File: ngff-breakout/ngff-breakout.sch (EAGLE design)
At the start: 43 parts, among them K1 694108106102, U1 IP4234CZ6, U2 LD1085D2T33R, X2 MINI-USB-SHIELD-UX60-MB-5ST

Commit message: ngff-breakout: intermediate state
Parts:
- removed C105, C109: 100u, rc-sysmocom:CAP_CERAMIC1206
- removed C106, C110: 100n, rc-sysmocom:CAP_CERAMIC_0603
- removed C107, C111: 33p, rc-sysmocom:CAP_CERAMIC_0402
- removed C108, C112: 10p, rc-sysmocom:CAP_CERAMIC_0603
- removed X4, X5: (no value), laforge:SMA-F-S-TH
- removed Y4, Y5: (no value), laforge:HRS_UFL
- added C12, C17: 10u, rc-sysmocom:CAP_CERAMIC_0805
- added C13: 100u, rc-sysmocom:CAP_CERAMIC1206
- added C14, C19: 100n, rc-sysmocom:CAP_CERAMIC_0603
- added C15: 33p, rc-sysmocom:CAP_CERAMIC_0402
- added C16: 10p, rc-sysmocom:CAP_CERAMIC_0603
- added C18: DNP, rcl:CPOL-EUSMCE
- added CN1: (no value), USB30B:USB3.0-B
- added CN2: (no value), USB30-MICROB:USB3.0-MICROB
- added X1: (no value), laforge:SMA-F-S-TH
- added Y1, Y2: (no value), laforge:HRS_UFL
- C1: value 10u -> 100n; device rc-sysmocom:CAP_CERAMIC_0805 -> rc-sysmocom:CAP_CERAMIC_0603; DESCRIPTION 10µF 16V Ceramic Capacitor X5R 0805 (2012 Metric) 0.079" L 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 -> CAP CER 0.1UF 16V 10% X7R 0603; LINK http://www.digikey.com/product-detail/en/samsung-electro-me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 -> http://www.digikey.com/product-detail/en/foo/1276-1005-1-ND; MANUFACTURER Samsung Electro-Mechanics America, Inc. -> Samsung Electro-Mechanics America, Inc; MANUFACTURERPARTNUMBER CL21A106KOQNNNG -> CL10B104KO8NNNC; ROHSCERTIFICATE UNKNOWN ROHS CERTIFICATE -> Bleifrei / RoHS-konform; SOURCEPARTNUMBER 1276-6455-1-ND -> 1276-1005-1-ND
- C10: value 100u -> 470u; device rc-sysmocom:CAP_CERAMIC1206 -> rcl:CPOL-EUUD-8X10; DESCRIPTION 100µF 6.3V Ceramic Capacitor X5R 1206 (3216 Metric) 0.126" 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 -> 470µF 6.3V Aluminum Capacitors Radial, Can - SMD 2000 Hrs @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; LINK http://www.digikey.com/product-detail/en/murata-electronics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 -> http://www.digikey.com/product-detail/en/nichicon/UUR0J471M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; MANUFACTURER Murata Electronics North America -> Nichicon; MANUFACTURERPARTNUMBER GRM31CR60J107ME39K -> UUR0J471MNL1GS; SOURCEPARTNUMBER 490-7217-1-ND -> 493-6207-1-ND
- C2: value 10u -> 33p; device rc-sysmocom:CAP_CERAMIC_0805 -> rc-sysmocom:CAP_CERAMIC_0402; DESCRIPTION 10µF 16V Ceramic Capacitor X5R 0805 (2012 Metric) 0.079" L 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 -> CAP CER 33PF 50V NP0 0402; LINK http://www.digikey.com/product-detail/en/samsung-electro-me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 -> http://www.digikey.com/product-detail/en/CL05C330JB5NNNC/12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; MANUFACTURERPARTNUMBER CL21A106KOQNNNG -> CL05C330JB5NNNC; ROHSCERTIFICATE UNKNOWN ROHS CERTIFICATE -> Bleifrei / RoHS-konform; SOURCEPARTNUMBER 1276-6455-1-ND -> 1276-1272-1-ND
- C3: value 470u -> 33p; device rcl:CPOL-EUUD-8X10 -> rc-sysmocom:CAP_CERAMIC_0402; DESCRIPTION 470µF 6.3V Aluminum Capacitors Radial, Can - SMD 2000 Hrs @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 -> CAP CER 33PF 50V NP0 0402; LINK http://www.digikey.com/product-detail/en/nichicon/UUR0J471M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 -> http://www.digikey.com/product-detail/en/CL05C330JB5NNNC/12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; MANUFACTURER Nichicon -> Samsung Electro-Mechanics America, Inc.; MANUFACTURERPARTNUMBER UUR0J471MNL1GS -> CL05C330JB5NNNC; ROHSCERTIFICATE UNKNOWN ROHS CERTIFICATE -> Bleifrei / RoHS-konform; SOURCEPARTNUMBER 493-6207-1-ND -> 1276-1272-1-ND
- C4: value DNP -> 33p; device rcl:CPOL-EUSMCE -> rc-sysmocom:CAP_CERAMIC_0402; DESCRIPTION NO DESCRIPTION -> CAP CER 33PF 50V NP0 0402; LINK UNKNOWN LINK -> http://www.digikey.com/product-detail/en/CL05C330JB5NNNC/12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; MANUFACTURER UNKNOWN MANUFACTURER -> Samsung Electro-Mechanics America, Inc.; MANUFACTURERPARTNUMBER UNKNOWN MANUFACTURER PART NUMBER -> CL05C330JB5NNNC; POPULATED FALSE -> TRUE; ROHSCERTIFICATE UNKNOWN ROHS CERTIFICATE -> Bleifrei / RoHS-konform; SOURCE UNKNOWN SOURCE -> DIGIKEY; SOURCEPARTNUMBER UNKNOWN SOURCE PART NUMBER -> 1276-1272-1-ND
- C5, C6: value 33p -> 100u; device rc-sysmocom:CAP_CERAMIC_0402 -> rc-sysmocom:CAP_CERAMIC1206; DESCRIPTION CAP CER 33PF 50V NP0 0402 -> 100µF 6.3V Ceramic Capacitor X5R 1206 (3216 Metric) 0.126" 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; LINK http://www.digikey.com/product-detail/en/CL05C330JB5NNNC/12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 -> http://www.digikey.com/product-detail/en/murata-electronics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; MANUFACTURER Samsung Electro-Mechanics America, Inc. -> Murata Electronics North America; MANUFACTURERPARTNUMBER CL05C330JB5NNNC -> GRM31CR60J107ME39K; ROHSCERTIFICATE Bleifrei / RoHS-konform -> UNKNOWN ROHS CERTIFICATE; SOURCEPARTNUMBER 1276-1272-1-ND -> 490-7217-1-ND
- C7: value 33p -> 100n; device rc-sysmocom:CAP_CERAMIC_0402 -> rc-sysmocom:CAP_CERAMIC_0603; DESCRIPTION CAP CER 33PF 50V NP0 0402 -> CAP CER 0.1UF 16V 10% X7R 0603; LINK http://www.digikey.com/product-detail/en/CL05C330JB5NNNC/12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 -> http://www.digikey.com/product-detail/en/foo/1276-1005-1-ND; MANUFACTURER Samsung Electro-Mechanics America, Inc. -> Samsung Electro-Mechanics America, Inc; MANUFACTURERPARTNUMBER CL05C330JB5NNNC -> CL10B104KO8NNNC; SOURCEPARTNUMBER 1276-1272-1-ND -> 1276-1005-1-ND
- C8: value 100n -> 33p; device rc-sysmocom:CAP_CERAMIC_0603 -> rc-sysmocom:CAP_CERAMIC_0402; DESCRIPTION CAP CER 0.1UF 16V 10% X7R 0603 -> CAP CER 33PF 50V NP0 0402; LINK http://www.digikey.com/product-detail/en/foo/1276-1005-1-ND -> http://www.digikey.com/product-detail/en/CL05C330JB5NNNC/12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; MANUFACTURER Samsung Electro-Mechanics America, Inc -> Samsung Electro-Mechanics America, Inc.; MANUFACTURERPARTNUMBER CL10B104KO8NNNC -> CL05C330JB5NNNC; SOURCEPARTNUMBER 1276-1005-1-ND -> 1276-1272-1-ND
- C9: value 100n -> 10p; DESCRIPTION CAP CER 0.1UF 16V 10% X7R 0603 -> CAP CER 10PF 50V NP0 0603; LINK http://www.digikey.com/product-detail/en/foo/1276-1005-1-ND -> http://www.digikey.com/product-detail/en/C0603C100J5GACTU/3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; MANUFACTURER Samsung Electro-Mechanics America, Inc -> Kemet; MANUFACTURERPARTNUMBER CL10B104KO8NNNC -> C0603C100J5GACTU; SOURCEPARTNUMBER 1276-1005-1-ND -> 399-1049-1-ND
- JP3: device jumper:JP2E -> pinhead:PINHD-2X12; DESCRIPTION NO DESCRIPTION -> 24 Positions Header, Unshrouded Connector 0.100" (2.54mm) T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; LINK UNKNOWN LINK -> http://www.digikey.com/product-detail/en/961224-6404-AR/3M9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; MANUFACTURER UNKNOWN MANUFACTURER -> 3M; MANUFACTURERPARTNUMBER UNKNOWN MANUFACTURER PART NUMBER -> 961224-6404-AR; SOURCE UNKNOWN SOURCE -> DIGIKEY; SOURCEPARTNUMBER UNKNOWN SOURCE PART NUMBER -> 3M9463-ND
- JP4: device pinhead:PINHD-2X12 -> jumper:JP2E; DESCRIPTION 24 Positions Header, Unshrouded Connector 0.100" (2.54mm) T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 -> NO DESCRIPTION; LINK http://www.digikey.com/product-detail/en/961224-6404-AR/3M9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 -> UNKNOWN LINK; MANUFACTURER 3M -> UNKNOWN MANUFACTURER; MANUFACTURERPARTNUMBER 961224-6404-AR -> UNKNOWN MANUFACTURER PART NUMBER; SOURCE DIGIKEY -> UNKNOWN SOURCE; SOURCEPARTNUMBER 3M9463-ND -> UNKNOWN SOURCE PART NUMBER
- LED1: value YELLOW -> GREEN
- LED2: value GREEN -> YELLOW
- R1, R2: value 47 -> 330; DESCRIPTION RES SMD 47 OHM 5% 1/10W 0603 -> RES SMD 330 OHM 5% 1/10W 0603; LINK http://www.digikey.com/product-detail/en/yageo/RC0603JR-074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 -> http://www.digikey.com/product-detail/en/yageo/RC0603JR-073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; MANUFACTURERPARTNUMBER RC0603JR-0747RL -> RC0603JR-07330RL; SOURCEPARTNUMBER 311-47GRCT-ND -> 311-330GRCT-ND
- R4: value 1M -> 47; DESCRIPTION RES SMD 1M OHM 5% 1/10W 0603 -> RES SMD 47 OHM 5% 1/10W 0603; LINK http://www.digikey.com/product-detail/en/yageo/RC0603JR-071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 -> http://www.digikey.com/product-detail/en/yageo/RC0603JR-074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; MANUFACTURERPARTNUMBER RC0603JR-071ML -> RC0603JR-0747RL; SOURCEPARTNUMBER 311-1.0MGRCT-ND -> 311-47GRCT-ND
- R5: value 330 -> 47; DESCRIPTION RES SMD 330 OHM 5% 1/10W 0603 -> RES SMD 47 OHM 5% 1/10W 0603; LINK http://www.digikey.com/product-detail/en/yageo/RC0603JR-073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 -> http://www.digikey.com/product-detail/en/yageo/RC0603JR-074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; MANUFACTURERPARTNUMBER RC0603JR-07330RL -> RC0603JR-0747RL; SOURCEPARTNUMBER 311-330GRCT-ND -> 311-47GRCT-ND
- R6: value 330 -> 1M; DESCRIPTION RES SMD 330 OHM 5% 1/10W 0603 -> RES SMD 1M OHM 5% 1/10W 0603; LINK http://www.digikey.com/product-detail/en/yageo/RC0603JR-073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 -> http://www.digikey.com/product-detail/en/yageo/RC0603JR-071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; MANUFACTURERPARTNUMBER RC0603JR-07330RL -> RC0603JR-071ML; SOURCEPARTNUMBER 311-330GRCT-ND -> 311-1.0MGRCT-ND
- X2: value MINI-USB-SHIELD-UX60-MB-5ST -> (none); device con-hirose:MINI-USB-SHIELD-UX60-MB-5ST -> laforge:SMA-F-S-TH; DESCRIPTION USB - mini B USB 2.0 Receptacle Connector 5 Position Surfac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 -> CONN SMA JACK STR 50 OHM PCB; LINK http://www.digikey.com/product-detail/en/hirose-electric-co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 -> http://www.digikey.com/product-detail/en/te-connectivity-am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; MANUFACTURER Hirose Electric Co Ltd -> TE Connectivity AMP Connectors; MANUFACTURERPARTNUMBER UX60-MB-5ST -> 5-1814832-1; SOURCEPARTNUMBER H2959CT-ND -> A97594-ND
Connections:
- removed net N$14 (its old number): X4.1, Y4.1
- new net N$11: CN1.TX+
- new net N$13: X2.1, Y2.1
- new net N$15: CN1.GND@1
- new net N$17: CN1.RX-
- new net N$18: CN1.RX+
- new net N$4: CN1.TX-
- new net USB3.0_RX_N: NGFF1G$1.USB3.0_RX_N
- new net USB3.0_RX_P: NGFF1G$1.USB3.0_RX_P
- new net USB3.0_TX_N: NGFF1G$1.USB3.0_TX_N
- new net USB3.0_TX_P: NGFF1G$1.USB3.0_TX_P
- net !CLKREQ: now also JP3.6; no longer JP4.6
- net COEX1: now also JP3.4; no longer JP4.4
- net COEX2: now also JP3.3; no longer JP4.3
- net GND: now also C10.-, C12.1, C13.1, C14.1, C15.2, C16.2, C17.1, C18.-, C19.1, C2.2, C3.2, C4.2, C5.1, C6.1, C7.1, C8.2, C9.2, CN1.GND@0, JP1.1, JP2.2, JP3.1, JP3.13, R1.1, R6.1, X1.GND@1, X1.GND@2, X1.GND@3, X1.GND@4, X2.GND@1, X2.GND@2, X2.GND@3, X2.GND@4, Y1.GND@1, Y1.GND@2, Y2.GND@1, Y2.GND@2; no longer C10.1, C105.1, C106.1, C107.2, C108.2, C109.1, C110.1, C111.2, C112.2, C2.1, C3.-, C4.-, C5.2, C6.2, C7.2, C8.1, C9.1, JP1.2, JP2.1, JP4.1, JP4.13, R4.1, R5.1, X2G$1.5, X4.GND@1, X4.GND@2, X4.GND@3, X4.GND@4, X5.GND@1, X5.GND@2, X5.GND@3, X5.GND@4, Y4.GND@1, Y4.GND@2, Y5.GND@1, Y5.GND@2
- net LDO_IN: now also C10.+, C12.2, JP4.2; no longer C1.2, C3.+, JP3.2
- net LED_WLAN: now also JP3.24; no longer JP4.24
- net LED_WPAN: now also JP3.23; no longer JP4.23
- net N$1: now also LED1.C, R1.2; no longer LED2.C, R5.2
- net N$10: now also C19.2, CN1.S1, CN1.S2, R6.2; no longer C9.2, R4.2, X2S.S1, X2S.S2, X2S.S3, X2S.S4
- net N$12: now also JP4.3; no longer JP3.3
- net N$16: now also JP3.11; no longer JP4.11
- net N$2: now also LED2.C, R2.1; no longer LED1.C, R6.1
- net N$3: now also R2.2; no longer R6.2
- net N$5: now also R5.1; no longer R1.1
- net N$7: now also X1.1, Y1.1; no longer X5.1, Y5.1
- net N$8: now also R3.1; no longer R2.1
- net N$9: now also R4.1; no longer R3.1
- net PERN0: now also JP3.9; no longer JP4.9
- net PERP0: now also JP3.12; no longer JP4.12
- net PERST: now also JP2.1; no longer JP1.1
- net PETN0: now also JP3.16; no longer JP4.16
- net PETP0: now also JP3.15; no longer JP4.15
- net REFCLK+: now also JP3.8; no longer JP4.8
- net REFCLK-: now also JP3.5; no longer JP4.5
- net RSVRD45: now also JP3.18; no longer JP4.18
- net RSVRD47: now also JP3.17; no longer JP4.17
- net RSVRD49: now also JP3.20; no longer JP4.20
- net RSVRD51: now also JP3.19; no longer JP4.19
- net SMB_CLK: now also JP3.21; no longer JP4.21
- net SMB_DATA: now also JP3.22; no longer JP4.22
- net UIM_C4: now also JP3.10; no longer JP4.10
- net UIM_C8: now also JP3.7; no longer JP4.7
- net USB_VBUS: now also CN1.VBUS, JP4.1; no longer JP3.1, X2G$1.1
- net USIM_CLK: now also C3.1, R3.2; no longer C5.1, R2.2
- net USIM_DATA: now also C4.1, R5.2; no longer C7.1, R1.2
- net USIM_POWER: now also C1.2; no longer C8.2
- net USIM_RESET: now also C2.1, R4.2; no longer C6.1, R3.2
- net VCC_3V3: now also C13.2, C14.2, C15.1, C16.1, C17.2, C18.+, C5.2, C6.2, C7.2, C8.1, C9.1, JP3.14; no longer C10.2, C105.2, C106.2, C107.1, C108.1, C109.2, C110.2, C111.1, C112.1, C2.2, C4.+, JP4.14
- net WAKE: now also JP3.2; no longer JP4.2
- net W_DISABLE: now also JP1.2; no longer JP2.2
- net _USB_D_N: now also CN1.D-; no longer X2G$1.2
- net _USB_D_P: now also CN1.D+; no longer X2G$1.3
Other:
- moved on the sheet: C1, C11, C2, C5, C6, C7, C8, C9, JP1, JP2, K1, LED1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

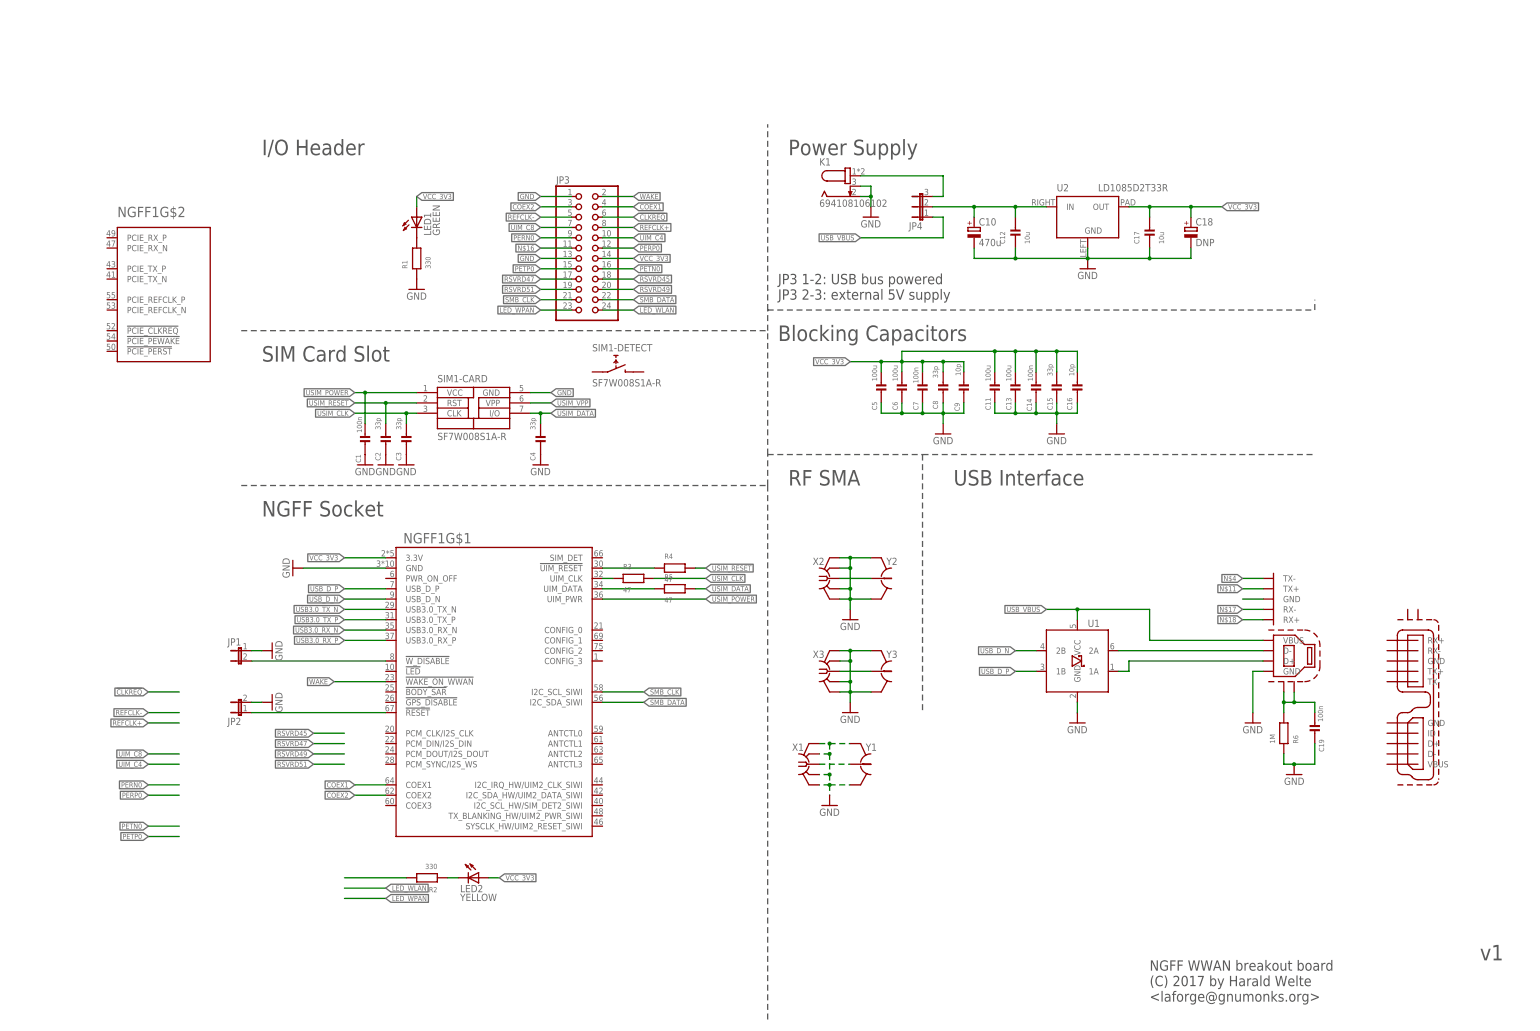
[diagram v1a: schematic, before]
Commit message: ngff-breakout: almost ready
missing: more vias, more ext. attributes (for BOM)
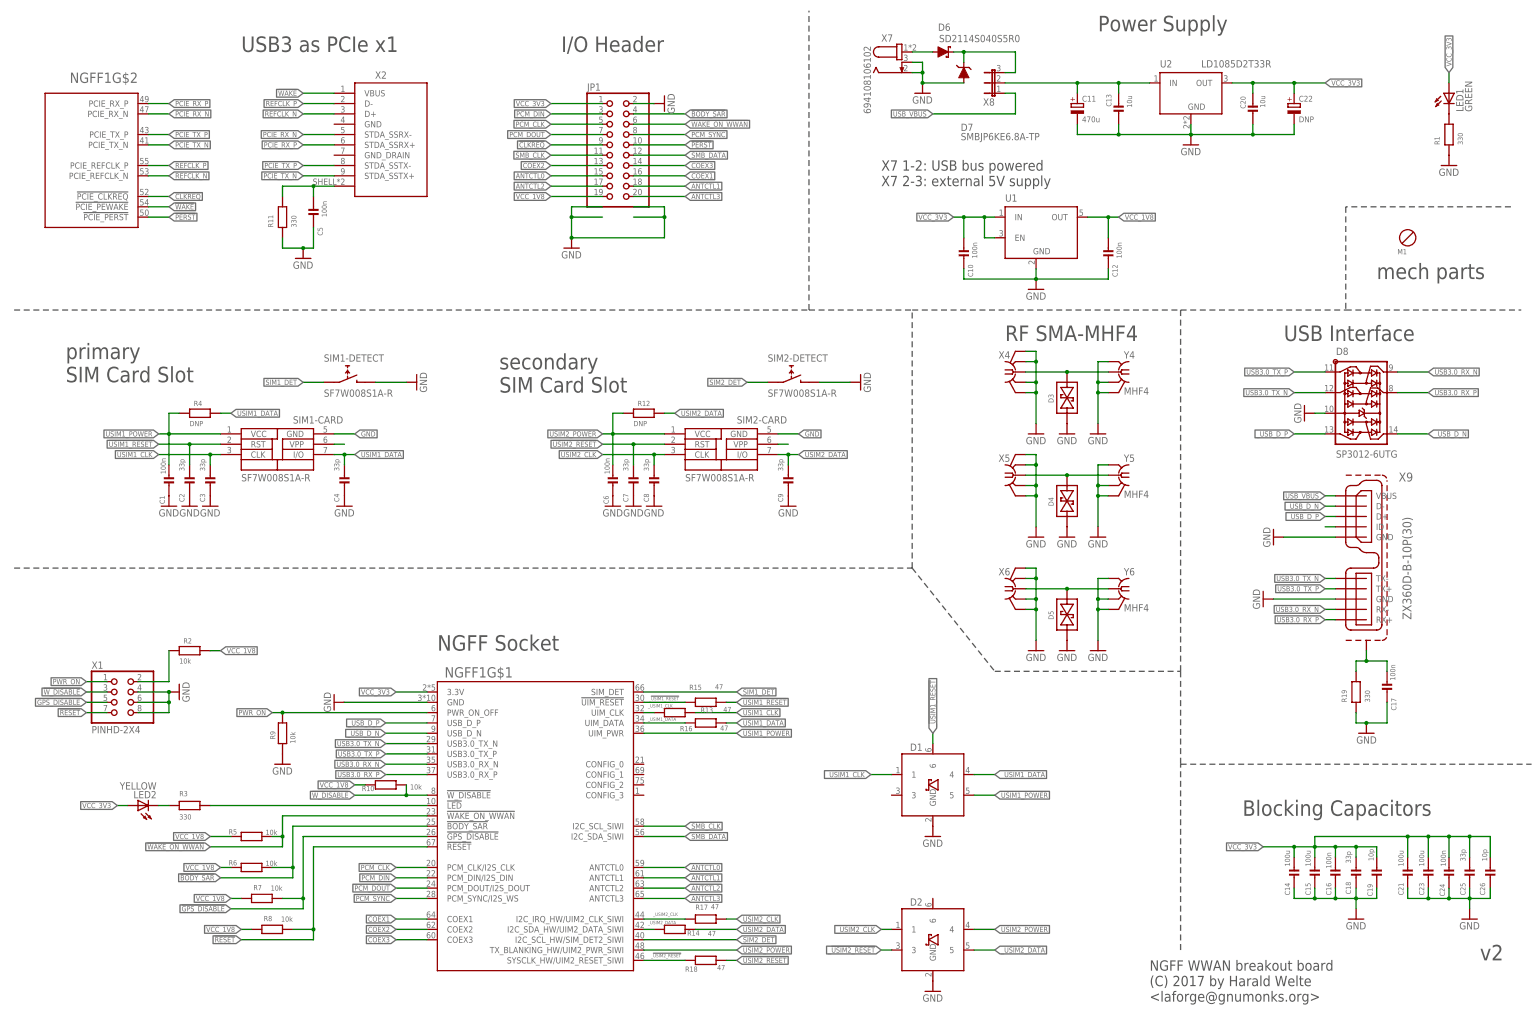
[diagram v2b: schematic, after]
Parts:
- removed CN1: (no value), USB30B:USB3.0-B
- removed CN2: (no value), USB30-MICROB:USB3.0-MICROB
- removed JP2: (no value), jumper:JP1E
- removed JP3: (no value), pinhead:PINHD-2X12
- removed JP4: (no value), jumper:JP2E
- removed K1: 694108106102, Wurth_Elektronik_Electromechanic_DC_Power_Jack_Connectors_rev15c:694108106102
- removed X3: (no value), laforge:SMA-F-S-TH
- removed Y1, Y2, Y3: (no value), laforge:HRS_UFL
- added C20: 10u, rc-sysmocom:CAP_CERAMIC_0805
- added C21, C23: 100u, rc-sysmocom:CAP_CERAMIC1206
- added C22: DNP, rcl:CPOL-EUSMCE
- added C24: 100n, rc-sysmocom:CAP_CERAMIC_0603
- added C25: 33p, rc-sysmocom:CAP_CERAMIC_0402
- added C26: 10p, rc-sysmocom:CAP_CERAMIC_0603
- added D1, D2: PESD5V0UBV, laforge:PESD5V0UBV
- added D3, D4, D5: GG040205170N2P, diodes-sysmocom:TVSDIODE-BIDI-0402
- added D6: SD2114S040S5R0, diodes-sysmocom:DIODE-SCHOTTKY-SMB
- added D7: SMBJP6KE6.8A-TP, diodes-sysmocom:DIODE-TVS-SMB
- added D8: SP3012-6UTG, SP3012:SP3012-6UTG
- added R10, R7, R8, R9: 10k, rc-sysmocom:RESISTOR_0603
- added R11, R19: 330, rc-sysmocom:RESISTOR_0603
- added R12: DNP, rc-sysmocom:RESISTOR_0603
- added R13, R14, R15, R16, R17, R18: 47, rc-sysmocom:RESISTOR_0402
- added SIM2: SF7W008S1A-R, SF7W008S1A-SIM:SF7W008S1A-R
- added X4, X5, X6: (no value), laforge:SMA-F-S-TH
- added X7: 694108106102, Wurth_Elektronik_Electromechanic_DC_Power_Jack_Connectors_rev15c:694108106102
- added X8: (no value), jumper:JP2E
- added X9: ZX360D-B-10P(30), USB30-MICROB:USB3.0-MICROB
- added Y4, Y5, Y6: MHF4, con-MHF4:MHF4
- C1: LINK http://www.digikey.com/product-detail/en/foo/1276-1005-1-ND -> http://www.digikey.de/product-detail/de/foo/1276-1005-1-ND
- C10: value 470u -> 100n; device rcl:CPOL-EUUD-8X10 -> rc-sysmocom:CAP_CERAMIC_0603; DESCRIPTION 470µF 6.3V Aluminum Capacitors Radial, Can - SMD 2000 Hrs @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 -> CAP CER 0.1UF 16V 10% X7R 0603; LINK http://www.digikey.com/product-detail/en/nichicon/UUR0J471M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 -> http://www.digikey.de/product-detail/de/foo/1276-1005-1-ND; MANUFACTURER Nichicon -> Samsung Electro-Mechanics America, Inc; MANUFACTURERPARTNUMBER UUR0J471MNL1GS -> CL10B104KO8NNNC; ROHSCERTIFICATE UNKNOWN ROHS CERTIFICATE -> Bleifrei / RoHS-konform; SOURCEPARTNUMBER 493-6207-1-ND -> 1276-1005-1-ND
- C11: value 100u -> 470u; device rc-sysmocom:CAP_CERAMIC1206 -> rcl:CPOL-EUUD-8X10; DESCRIPTION 100µF 6.3V Ceramic Capacitor X5R 1206 (3216 Metric) 0.126" 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 -> CAP ALUM 470UF 20%% 6.3V SMD; LINK http://www.digikey.com/product-detail/en/murata-electronics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 -> http://www.digikey.de/product-detail/de/nichicon/UUR0J471MN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; MANUFACTURER Murata Electronics North America -> Nichicon; MANUFACTURERPARTNUMBER GRM31CR60J107ME39K -> UUR0J471MNL1GS; ROHSCERTIFICATE UNKNOWN ROHS CERTIFICATE -> Bleifrei / RoHS-konform; SOURCEPARTNUMBER 490-7217-1-ND -> 493-6207-1-ND
- C12, C17: value 10u -> 100n; device rc-sysmocom:CAP_CERAMIC_0805 -> rc-sysmocom:CAP_CERAMIC_0603; DESCRIPTION 10µF 16V Ceramic Capacitor X5R 0805 (2012 Metric) 0.079" L 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 -> CAP CER 0.1UF 16V 10% X7R 0603; LINK http://www.digikey.com/product-detail/en/samsung-electro-me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 -> http://www.digikey.de/product-detail/de/foo/1276-1005-1-ND; MANUFACTURER Samsung Electro-Mechanics America, Inc. -> Samsung Electro-Mechanics America, Inc; MANUFACTURERPARTNUMBER CL21A106KOQNNNG -> CL10B104KO8NNNC; ROHSCERTIFICATE UNKNOWN ROHS CERTIFICATE -> Bleifrei / RoHS-konform; SOURCEPARTNUMBER 1276-6455-1-ND -> 1276-1005-1-ND
- C13: value 100u -> 10u; device rc-sysmocom:CAP_CERAMIC1206 -> rc-sysmocom:CAP_CERAMIC_0805; DESCRIPTION 100µF 6.3V Ceramic Capacitor X5R 1206 (3216 Metric) 0.126" 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 -> CAP CER 10UF 16V X5R 0805; LINK http://www.digikey.com/product-detail/en/murata-electronics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 -> http://www.digikey.de/product-detail/de/samsung-electro-mec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; MANUFACTURER Murata Electronics North America -> Samsung Electro-Mechanics; MANUFACTURERPARTNUMBER GRM31CR60J107ME39K -> CL21A106KOQNNNG; ROHSCERTIFICATE UNKNOWN ROHS CERTIFICATE -> Bleifrei / RoHS-konform; SOURCEPARTNUMBER 490-7217-1-ND -> 1276-6455-1-ND
- C14: value 100n -> 100u; device rc-sysmocom:CAP_CERAMIC_0603 -> rc-sysmocom:CAP_CERAMIC1206; DESCRIPTION CAP CER 0.1UF 16V 10% X7R 0603 -> CAP CER 100UF 6.3V X5R 1206; LINK http://www.digikey.com/product-detail/en/foo/1276-1005-1-ND -> http://www.digikey.de/product-detail/de/murata-electronics-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; MANUFACTURER Samsung Electro-Mechanics America, Inc -> Murata Electronics North America; MANUFACTURERPARTNUMBER CL10B104KO8NNNC -> GRM31CR60J107ME39K; SOURCEPARTNUMBER 1276-1005-1-ND -> 490-7217-1-ND
- C15: value 33p -> 100u; device rc-sysmocom:CAP_CERAMIC_0402 -> rc-sysmocom:CAP_CERAMIC1206; DESCRIPTION CAP CER 33PF 50V NP0 0402 -> CAP CER 100UF 6.3V X5R 1206; LINK http://www.digikey.com/product-detail/en/CL05C330JB5NNNC/12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 -> http://www.digikey.de/product-detail/de/murata-electronics-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; MANUFACTURER Samsung Electro-Mechanics America, Inc. -> Murata Electronics North America; MANUFACTURERPARTNUMBER CL05C330JB5NNNC -> GRM31CR60J107ME39K; SOURCEPARTNUMBER 1276-1272-1-ND -> 490-7217-1-ND
- C16: value 10p -> 100n; DESCRIPTION CAP CER 10PF 50V NP0 0603 -> CAP CER 0.1UF 16V 10% X7R 0603; LINK http://www.digikey.com/product-detail/en/C0603C100J5GACTU/3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 -> http://www.digikey.de/product-detail/de/foo/1276-1005-1-ND; MANUFACTURER Kemet -> Samsung Electro-Mechanics America, Inc; MANUFACTURERPARTNUMBER C0603C100J5GACTU -> CL10B104KO8NNNC; SOURCEPARTNUMBER 399-1049-1-ND -> 1276-1005-1-ND
- C18: value DNP -> 33p; device rcl:CPOL-EUSMCE -> rc-sysmocom:CAP_CERAMIC_0402; DESCRIPTION NO DESCRIPTION -> CAP CER 33PF 50V NP0 0402; LINK UNKNOWN LINK -> http://www.digikey.de/product-detail/de/CL05C330JB5NNNC/127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; MANUFACTURER UNKNOWN MANUFACTURER -> Samsung Electro-Mechanics America, Inc.; MANUFACTURERPARTNUMBER UNKNOWN MANUFACTURER PART NUMBER -> CL05C330JB5NNNC; POPULATED FALSE -> TRUE; ROHSCERTIFICATE UNKNOWN ROHS CERTIFICATE -> Bleifrei / RoHS-konform; SOURCE UNKNOWN SOURCE -> DIGIKEY; SOURCEPARTNUMBER UNKNOWN SOURCE PART NUMBER -> 1276-1272-1-ND
- C19: value 100n -> 10p; DESCRIPTION CAP CER 0.1UF 16V 10% X7R 0603 -> CAP CER 10PF 50V NP0 0603; LINK http://www.digikey.com/product-detail/en/foo/1276-1005-1-ND -> http://www.digikey.de/product-detail/de/C0603C100J5GACTU/39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; MANUFACTURER Samsung Electro-Mechanics America, Inc -> Kemet; MANUFACTURERPARTNUMBER CL10B104KO8NNNC -> C0603C100J5GACTU; SOURCEPARTNUMBER 1276-1005-1-ND -> 399-1049-1-ND
- C2, C3, C4, C8: LINK http://www.digikey.com/product-detail/en/CL05C330JB5NNNC/12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 -> http://www.digikey.de/product-detail/de/CL05C330JB5NNNC/127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
- C5, C6: value 100u -> 100n; device rc-sysmocom:CAP_CERAMIC1206 -> rc-sysmocom:CAP_CERAMIC_0603; DESCRIPTION 100µF 6.3V Ceramic Capacitor X5R 1206 (3216 Metric) 0.126" 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 -> CAP CER 0.1UF 16V 10% X7R 0603; LINK http://www.digikey.com/product-detail/en/murata-electronics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 -> http://www.digikey.de/product-detail/de/foo/1276-1005-1-ND; MANUFACTURER Murata Electronics North America -> Samsung Electro-Mechanics America, Inc; MANUFACTURERPARTNUMBER GRM31CR60J107ME39K -> CL10B104KO8NNNC; ROHSCERTIFICATE UNKNOWN ROHS CERTIFICATE -> Bleifrei / RoHS-konform; SOURCEPARTNUMBER 490-7217-1-ND -> 1276-1005-1-ND
- C7: value 100n -> 33p; device rc-sysmocom:CAP_CERAMIC_0603 -> rc-sysmocom:CAP_CERAMIC_0402; DESCRIPTION CAP CER 0.1UF 16V 10% X7R 0603 -> CAP CER 33PF 50V NP0 0402; LINK http://www.digikey.com/product-detail/en/foo/1276-1005-1-ND -> http://www.digikey.de/product-detail/de/CL05C330JB5NNNC/127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; MANUFACTURER Samsung Electro-Mechanics America, Inc -> Samsung Electro-Mechanics America, Inc.; MANUFACTURERPARTNUMBER CL10B104KO8NNNC -> CL05C330JB5NNNC; SOURCEPARTNUMBER 1276-1005-1-ND -> 1276-1272-1-ND
- C9: value 10p -> 33p; device rc-sysmocom:CAP_CERAMIC_0603 -> rc-sysmocom:CAP_CERAMIC_0402; DESCRIPTION CAP CER 10PF 50V NP0 0603 -> CAP CER 33PF 50V NP0 0402; LINK http://www.digikey.com/product-detail/en/C0603C100J5GACTU/3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 -> http://www.digikey.de/product-detail/de/CL05C330JB5NNNC/127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; MANUFACTURER Kemet -> Samsung Electro-Mechanics America, Inc.; MANUFACTURERPARTNUMBER C0603C100J5GACTU -> CL05C330JB5NNNC; SOURCEPARTNUMBER 399-1049-1-ND -> 1276-1272-1-ND
- JP1: device jumper:JP1E -> laforge:PINHD-2X10; CLASS CONNECTOR\JUMPER -> (none); DESCRIPTION NO DESCRIPTION -> (none); LINK UNKNOWN LINK -> (none); MANUFACTURER UNKNOWN MANUFACTURER -> (none); MANUFACTURERPARTNUMBER UNKNOWN MANUFACTURER PART NUMBER -> (none); POPULATED TRUE -> (none); ROHSCERTIFICATE UNKNOWN ROHS CERTIFICATE -> (none); SOURCE UNKNOWN SOURCE -> (none); SOURCEPARTNUMBER UNKNOWN SOURCE PART NUMBER -> (none)
- NGFF1: CLASS (none) -> UNKNOWN CLASS; DESCRIPTION (none) -> NO DESCRIPTION; LINK (none) -> UNKNOWN LINK; MANUFACTURER (none) -> UNKNOWN MANUFACTURER; MANUFACTURERPARTNUMBER (none) -> UNKNOWN MANUFACTURER PART NUMBER; POPULATED (none) -> TRUE; ROHSCERTIFICATE (none) -> UNKNOWN ROHS CERTIFICATE; SOURCE (none) -> UNKNOWN SOURCE; SOURCEPARTNUMBER (none) -> UNKNOWN SOURCE PART NUMBER
- R1: DESCRIPTION RES SMD 330 OHM 5% 1/10W 0603 -> RES SMD 330 OHM 5%% 1/10W 0603; LINK http://www.digikey.com/product-detail/en/yageo/RC0603JR-073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 -> http://www.digikey.de/product-detail/de/yageo/RC0603JR-0733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; ROHSCERTIFICATE UNKNOWN ROHS CERTIFICATE -> Bleifrei / RoHS-konform
- R2: value 330 -> 10k; DESCRIPTION RES SMD 330 OHM 5% 1/10W 0603 -> RES 10K OHM 1%% 1/10W 0603; LINK http://www.digikey.com/product-detail/en/yageo/RC0603JR-073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 -> https://www.digikey.de/product-detail/de/stackpole-electron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; MANUFACTURER Yageo -> Stackpole Electronics Inc; MANUFACTURERPARTNUMBER RC0603JR-07330RL -> RMCF0603FT10K0; SOURCEPARTNUMBER 311-330GRCT-ND -> RMCF0603FT10K0CT-ND
- R3: value 47 -> 330; DESCRIPTION RES SMD 47 OHM 5% 1/10W 0603 -> RES SMD 330 OHM 5%% 1/10W 0603; LINK http://www.digikey.com/product-detail/en/yageo/RC0603JR-074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 -> http://www.digikey.de/product-detail/de/yageo/RC0603JR-0733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; MANUFACTURERPARTNUMBER RC0603JR-0747RL -> RC0603JR-07330RL; ROHSCERTIFICATE UNKNOWN ROHS CERTIFICATE -> Bleifrei / RoHS-konform; SOURCEPARTNUMBER 311-47GRCT-ND -> 311-330GRCT-ND
- R4: value 47 -> DNP; DESCRIPTION RES SMD 47 OHM 5% 1/10W 0603 -> RES 10K OHM 1%% 1/10W 0603; LINK http://www.digikey.com/product-detail/en/yageo/RC0603JR-074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 -> https://www.digikey.de/product-detail/de/stackpole-electron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; MANUFACTURER Yageo -> Stackpole Electronics Inc; MANUFACTURERPARTNUMBER RC0603JR-0747RL -> RMCF0603FT10K0; SOURCEPARTNUMBER 311-47GRCT-ND -> RMCF0603FT10K0CT-ND
- R5: value 47 -> 10k; DESCRIPTION RES SMD 47 OHM 5% 1/10W 0603 -> RES 10K OHM 1%% 1/10W 0603; LINK http://www.digikey.com/product-detail/en/yageo/RC0603JR-074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 -> https://www.digikey.de/product-detail/de/stackpole-electron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; MANUFACTURER Yageo -> Stackpole Electronics Inc; MANUFACTURERPARTNUMBER RC0603JR-0747RL -> RMCF0603FT10K0; SOURCEPARTNUMBER 311-47GRCT-ND -> RMCF0603FT10K0CT-ND
- R6: value 1M -> 10k; DESCRIPTION RES SMD 1M OHM 5% 1/10W 0603 -> RES 10K OHM 1%% 1/10W 0603; LINK http://www.digikey.com/product-detail/en/yageo/RC0603JR-071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 -> https://www.digikey.de/product-detail/de/stackpole-electron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; MANUFACTURER Yageo -> Stackpole Electronics Inc; MANUFACTURERPARTNUMBER RC0603JR-071ML -> RMCF0603FT10K0; SOURCEPARTNUMBER 311-1.0MGRCT-ND -> RMCF0603FT10K0CT-ND
- SIM1: DESCRIPTION 8 (6 + 2) Position Card Connector SIM Card Surface Mount, R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 -> CONN SIM CARD HINGED TYPE R/A; LINK http://www.digikey.com/product-detail/en/jae-electronics/SF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 -> http://www.digikey.de/product-detail/de/jae-electronics/SF7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; ROHSCERTIFICATE UNKNOWN ROHS CERTIFICATE -> Bleifrei / RoHS-konform
- U1: value IP4234CZ6 -> (none); device laforge:IP4234CZ6 -> ldo:LDO_FIXED_EN-MIC5365-YC5; DESCRIPTION TVS DIODE 5.5VWM 6TSOP -> NO DESCRIPTION; LINK http://www.digikey.com/product-detail/en/nxp-semiconductors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 -> UNKNOWN LINK; MANUFACTURER NXP Semiconductors -> UNKNOWN MANUFACTURER; MANUFACTURERPARTNUMBER IP4234CZ6,125 -> UNKNOWN MANUFACTURER PART NUMBER; SOURCE DIGIKEY -> UNKNOWN SOURCE; SOURCEPARTNUMBER 568-5869-1-ND -> UNKNOWN SOURCE PART NUMBER
- U2: device ldo:LDO-LD1085D2 -> ldo:LDO-MCP1827S; DESCRIPTION Linear Voltage Regulator IC Positive Fixed 1 Output 3.3V 3A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 -> IC REG LINEAR 3.3V 3A D2PAK; LINK http://www.digikey.com/product-detail/en/stmicroelectronics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 -> http://www.digikey.de/product-detail/de/stmicroelectronics/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; ROHSCERTIFICATE UNKNOWN ROHS CERTIFICATE -> Bleifrei / RoHS-konform
- X1: value (none) -> PINHD-2X4; device laforge:SMA-F-S-TH -> laforge:PINHD-2X4; CLASS CONNECTOR -> CONNECTOR\JUMPER; DESCRIPTION CONN SMA JACK STR 50 OHM PCB -> NO DESCRIPTION; LINK http://www.digikey.com/product-detail/en/te-connectivity-am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 -> UNKNOWN LINK; MANUFACTURER TE Connectivity AMP Connectors -> UNKNOWN MANUFACTURER; MANUFACTURERPARTNUMBER 5-1814832-1 -> UNKNOWN MANUFACTURER PART NUMBER; SOURCE DIGIKEY -> UNKNOWN SOURCE; SOURCEPARTNUMBER A97594-ND -> UNKNOWN SOURCE PART NUMBER
- X2: device laforge:SMA-F-S-TH -> InputOutputIO (rev19a):692121030100; CLASS CONNECTOR -> CONNECTOR\JUMPER; DESCRIPTION CONN SMA JACK STR 50 OHM PCB -> NO DESCRIPTION; LINK http://www.digikey.com/product-detail/en/te-connectivity-am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 -> UNKNOWN LINK; MANUFACTURER TE Connectivity AMP Connectors -> UNKNOWN MANUFACTURER; MANUFACTURERPARTNUMBER 5-1814832-1 -> UNKNOWN MANUFACTURER PART NUMBER; SOURCE DIGIKEY -> UNKNOWN SOURCE; SOURCEPARTNUMBER A97594-ND -> UNKNOWN SOURCE PART NUMBER
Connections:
- net USIM_VPP renamed N$8
- removed net LED_WLAN: JP3.24
- removed net LED_WPAN: JP3.23
- removed net N$11: CN1.TX+
- removed net N$15: CN1.GND@1
- removed net N$16: JP3.11
- removed net N$8 (its old number): NGFF1G$1.UIM_CLK, R3.1
- removed net N$9: NGFF1G$1.!UIM_RESET, R4.1
- removed net PERN0: JP3.9
- removed net PERP0: JP3.12
- removed net PERST: JP2.1, NGFF1G$1.!RESET
- removed net PETN0: JP3.16
- removed net PETP0: JP3.15
- removed net REFCLK+: JP3.8
- removed net REFCLK-: JP3.5
- removed net RSVRD45: JP3.18
- removed net RSVRD47: JP3.17
- removed net RSVRD49: JP3.20
- removed net RSVRD51: JP3.19
- removed net UIM_C4: JP3.10
- removed net UIM_C8: JP3.7
- removed net USB_D_N: NGFF1G$1.USB_D_N, U1.2B
- removed net USB_D_P: NGFF1G$1.USB_D_P, U1.1B
- removed net USIM_CLK: C3.1, R3.2, SIM1-CARD.CLK
- removed net USIM_DATA: C4.1, R5.2, SIM1-CARD.I/O
- removed net USIM_POWER: C1.2, NGFF1G$1.UIM_PWR, SIM1-CARD.VCC
- removed net USIM_RESET: C2.1, R4.2, SIM1-CARD.RST
- removed net WAKE: JP3.2, NGFF1G$1.!WAKE_ON_WWAN
- removed net W_DISABLE: JP1.2, NGFF1G$1.!W_DISABLE
- new net !BODY_SAR: JP1.4, NGFF1G$1.!BODY_SAR, R6.1
- new net !GPS_DISABLE: NGFF1G$1.!GPS_DISABLE, R7.1, X1.5
- new net !PERST: JP1.10, NGFF1G$2.!PCIE_PERST
- new net !RESET: NGFF1G$1.!RESET, R8.1, X1.7
- new net !USIM1_RESET: C2.1, R15.2, SIM1-CARD.RST
- new net !USIM2_RESET: C7.1, R18.2, SIM2-CARD.RST
- new net !WAKE: NGFF1G$2.!PCIE_PEWAKE, X2.VBUS
- new net !WAKE_ON_WWAN: JP1.6, NGFF1G$1.!WAKE_ON_WWAN, R5.1
- new net !W_DISABLE: NGFF1G$1.!W_DISABLE, R10.1, X1.3
- new net ANTCTL0: JP1.15, NGFF1G$1.ANTCTL0
- new net ANTCTL1: JP1.18, NGFF1G$1.ANTCTL1
- new net ANTCTL2: JP1.17, NGFF1G$1.ANTCTL2
- new net ANTCTL3: JP1.20, NGFF1G$1.ANTCTL3
- new net COEX3: JP1.14, NGFF1G$1.COEX3
- new net N$6: NGFF1G$1.!LED, R3.2
- new net PCIE_RX_N: NGFF1G$2.PCIE_RX_N, X2.STDA_SSRX-
- new net PCIE_RX_P: NGFF1G$2.PCIE_RX_P, X2.STDA_SSRX+
- new net PCIE_TX_N: NGFF1G$2.PCIE_TX_N, X2.STDA_SSTX+
- new net PCIE_TX_P: NGFF1G$2.PCIE_TX_P, X2.STDA_SSTX-
- new net PCM_CLK: JP1.5, NGFF1G$1.PCM_CLK/I2S_CLK
- new net PCM_DIN: JP1.3, NGFF1G$1.PCM_DIN/I2S_DIN
- new net PCM_DOUT: JP1.7, NGFF1G$1.PCM_DOUT/I2S_DOUT
- new net PCM_SYNC: JP1.8, NGFF1G$1.PCM_SYNC/I2S_WS
- new net PWR_ON: NGFF1G$1.PWR_ON_OFF, R9.2, X1.1
- new net REFCLK_N: NGFF1G$2.PCIE_REFCLK_N, X2.D+
- new net REFCLK_P: NGFF1G$2.PCIE_REFCLK_P, X2.D-
- new net SIM1_DET: NGFF1G$1.SIM_DET, SIM1-DETECT.0@A
- new net SIM2_DET: NGFF1G$1.I2C_SCL_HW/SIM_DET2_SIWI, SIM2-DETECT.0@A
- new net USIM1_CLK: C3.1, R13.2, SIM1-CARD.CLK
- new net USIM1_DATA: C4.1, R16.2, R4.2, SIM1-CARD.I/O
- new net USIM1_POWER: C1.2, D1.5, NGFF1G$1.UIM_PWR, R4.1, SIM1-CARD.VCC
- new net USIM2_CLK: C8.1, R17.2, SIM2-CARD.CLK
- new net USIM2_DATA: C9.1, R12.2, R14.2, SIM2-CARD.I/O
- new net USIM2_POWER: C6.2, D2.4, NGFF1G$1.TX_BLANKING_HW/UIM2_PWR_SIWI, R12.1, SIM2-CARD.VCC
- new net VCC_1V8: C12.2, JP1.19, R10.2, R2.2, R5.2, R6.2, R7.2, R8.2, U1.OUT
- new net _!USIM1_RESET: D1.6, NGFF1G$1.!UIM_RESET, R15.1
- new net _!USIM2_RESET: D2.3, NGFF1G$1.SYSCLK_HW/UIM2_RESET_SIWI, R18.1
- new net _USIM1_CLK: D1.1, NGFF1G$1.UIM_CLK, R13.1
- new net _USIM1_DATA: D1.4, NGFF1G$1.UIM_DATA, R16.1
- new net _USIM2_CLK: D2.1, NGFF1G$1.I2C_IRQ_HW/UIM2_CLK_SIWI, R17.1
- new net _USIM2_DATA: D2.5, NGFF1G$1.I2C_SDA_HW/UIM2_DATA_SIWI, R14.1
- net !CLKREQ: now also JP1.9, NGFF1G$2.!PCIE_CLKREQ; no longer JP3.6
- net COEX1: now also JP1.16; no longer JP3.4
- net COEX2: now also JP1.13; no longer JP3.3
- net GND: now also C10.1, C11.-, C15.1, C16.1, C18.2, C19.2, C20.1, C21.1, C22.-, C23.1, C24.1, C25.2, C26.2, C7.2, D1.GND, D2.GND, D3.P$1, D4.P$1, D5.P$1, D7.A, D8.GND, JP1.2, R11.1, R19.1, R9.1, SIM1-DETECT.1@A, SIM2-CARD.GND, SIM2-DETECT.1@A, X1.4, X1.6, X1.8, X4.GND@1, X4.GND@2, X4.GND@3, X4.GND@4, X5.GND@1, X5.GND@2, X5.GND@3, X5.GND@4, X6.GND@1, X6.GND@2, X6.GND@3, X6.GND@4, X7.2, X7.3, X9.GND@0, X9.GND@1, Y4.GND@2, Y4.GND@3, Y4.GND@4, Y5.GND@2, Y5.GND@3, Y5.GND@4, Y6.GND@2, Y6.GND@3, Y6.GND@4; no longer C10.-, C11.1, C15.2, C16.2, C18.-, C19.1, C7.1, CN1.GND@0, JP1.1, JP2.2, JP3.1, JP3.13, K1.2, K1.3, R6.1, X1.GND@1, X1.GND@2, X1.GND@3, X1.GND@4, X2.GND@1, X2.GND@2, X2.GND@3, X2.GND@4, X3.GND@1, X3.GND@2, X3.GND@3, X3.GND@4, Y1.GND@1, Y1.GND@2, Y2.GND@1, Y2.GND@2, Y3.GND@1, Y3.GND@2
- net LDO_IN: now also C11.+, C13.2, X8.2; no longer C10.+, C12.2, JP4.2
- net N$10: now also C17.2, R19.2, X9.S1; no longer C19.2, CN1.S1, CN1.S2, R6.2
- net N$12: now also D6.C, D7.C, X8.3; no longer JP4.3, K1.1
- net N$13: now also D3.P$2, X4.1, Y4.1; no longer X2.1, Y2.1
- net N$14: now also D4.P$2, X5.1, Y5.1; no longer X3.1, Y3.1
- net N$17: now also X9.ID; no longer CN1.RX-
- net N$18: now also R2.1, X1.2; no longer CN1.RX+
- net N$2: now also R3.1; no longer R2.1
- net N$3: now also D6.A, X7.1; no longer R2.2
- net N$4: now also C5.2, R11.2, X2.SHIELD; no longer CN1.TX-
- net N$5: now also SIM2-CARD.VPP; no longer NGFF1G$1.UIM_DATA, R5.1
- net N$7: now also D5.P$2, X6.1, Y6.1; no longer X1.1, Y1.1
- net SMB_CLK: now also JP1.11; no longer JP3.21
- net SMB_DATA: now also JP1.12; no longer JP3.22
- net USB3.0_RX_N: now also D8.7, X9.RX-
- net USB3.0_RX_P: now also D8.6, X9.RX+
- net USB3.0_TX_N: now also D8.2, X9.TX-
- net USB3.0_TX_P: now also D8.1, X9.TX+
- net USB_VBUS: now also X8.1, X9.VBUS; no longer CN1.VBUS, JP4.1, U1.VCC
- net VCC_3V3: now also C10.2, C15.2, C16.2, C18.1, C19.1, C20.2, C21.2, C22.+, C23.2, C24.2, C25.1, C26.1, JP1.1, U1.EN, U1.IN; no longer C11.2, C13.2, C15.1, C16.1, C17.2, C18.+, C5.2, C6.2, C7.2, C8.1, C9.1, JP3.14
- net _USB_D_N: now also D8.5, NGFF1G$1.USB_D_N, X9.D-; no longer CN1.D-, U1.2A
- net _USB_D_P: now also D8.4, NGFF1G$1.USB_D_P, X9.D+; no longer CN1.D+, U1.1A
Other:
- note added: "RF SMA-MHF4"
- note added: "USB3 as PCIe x1"
- note added: "X7 1-2: USB bus powered X7 2-3: external 5V supply"
- note added: "mech parts"
- note added: "primary SIM Card Slot"
- note added: "secondary SIM Card Slot"
- note removed: "JP3 1-2: USB bus powered JP3 2-3: external 5V supply"
- note removed: "RF SMA"
- note removed: "SIM Card Slot"
- moved on the sheet: C1, C12, C13, C14, C15, C16, C17, C19, C2, C3, C4, C5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

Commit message: ngff: finishing work
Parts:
- added JP501, JP502: FIDUCIALUFIDUCIAL, SparkFun:FIDUCIALUFIDUCIAL
- JP1: CLASS (none) -> CONNECTOR\JUMPER; DESCRIPTION (none) -> NO DESCRIPTION; LINK (none) -> UNKNOWN LINK; MANUFACTURER (none) -> UNKNOWN MANUFACTURER; MANUFACTURERPARTNUMBER (none) -> UNKNOWN MANUFACTURER PART NUMBER; POPULATED (none) -> TRUE; ROHSCERTIFICATE (none) -> UNKNOWN ROHS CERTIFICATE; SOURCE (none) -> UNKNOWN SOURCE; SOURCEPARTNUMBER (none) -> UNKNOWN SOURCE PART NUMBER
- NGFF1: LINK UNKNOWN LINK -> https://www.digikey.de/product-detail/de/te-connectivity-am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
